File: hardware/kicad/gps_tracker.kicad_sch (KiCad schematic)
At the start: 16 parts, among them J1 GNSS: Foxeer M10Q-250 / Beiti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, J2 BIGGA GSM (SIM800C) board, J3 SSD1306 0.96" OLED I2C 0x3C, J4 MicroSD SPI module, J5 Battery Shield V8, 2x18650, J6 BMA400 CJMCU-400, J7 Button module, U1 ESP32-S3 SuperMini (ESP32-S3F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

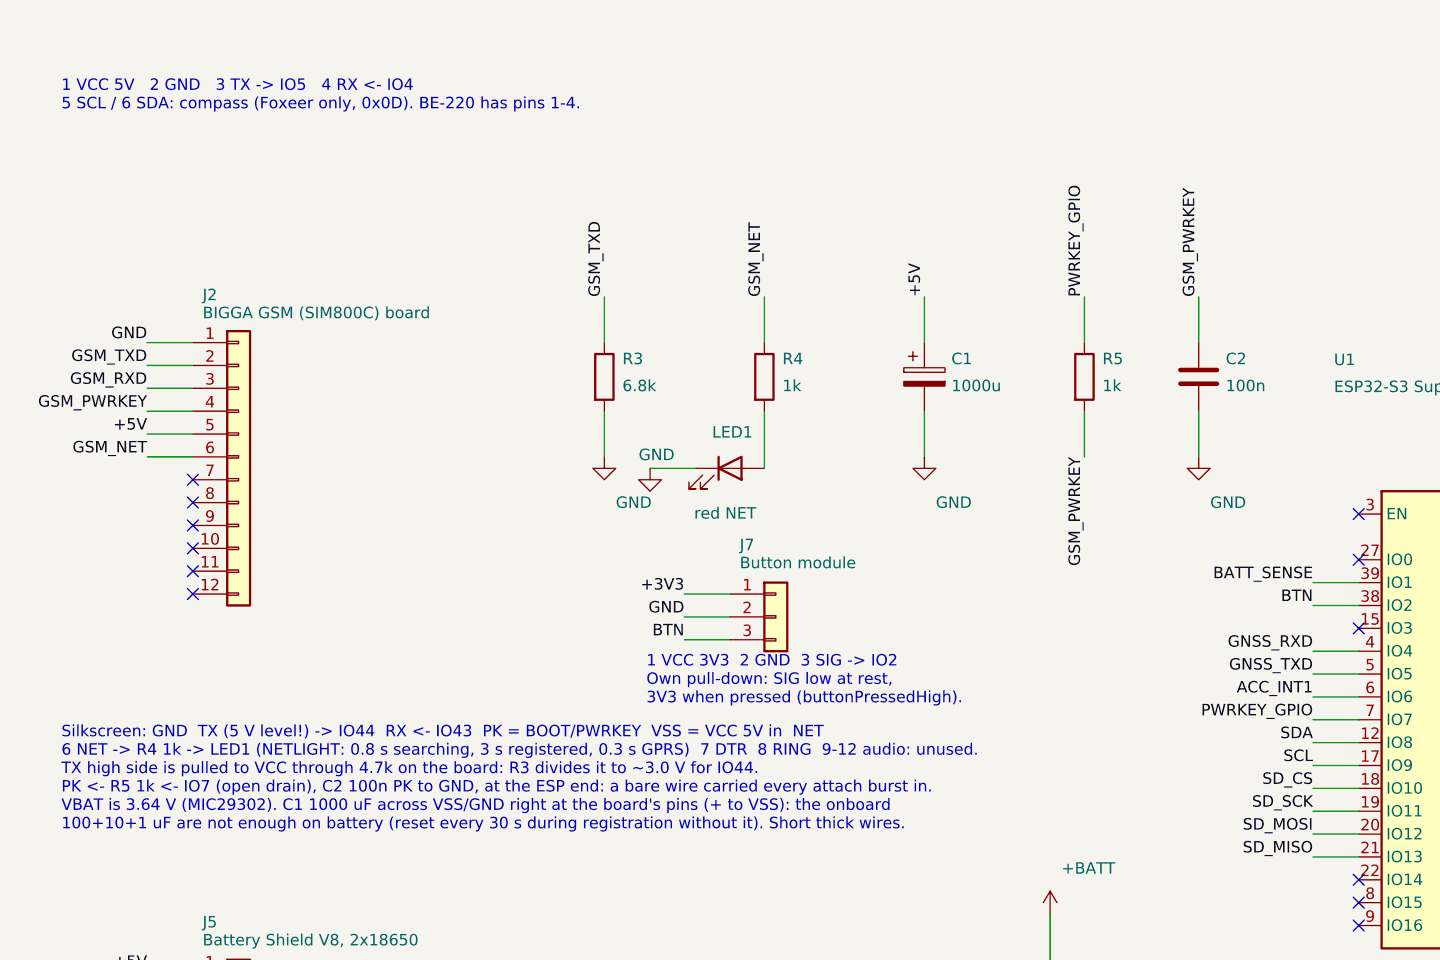
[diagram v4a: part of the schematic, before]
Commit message: Modem PWRKEY driven through an NPN transistor; drawings and documents follow
GPIO7 now drives the base of a 2N2222A through 10 kΩ, with 100 kΩ from
base to GND to keep it off while the ESP boots or sleeps; the emitter is
on GND and the collector pulls the modem's PWRKEY down. SIMCom's hardware
guide recommends this drive: nothing from the modem's line, neither the
attach bursts nor its ~4 V pull-up, reaches the ESP32 pin. Verified on
the bench with the modem powered off first: key pulse, 'Modem answered',
a fresh GPRS attach, no resets.

Config::gsmPowerKeyViaTransistor (true) inverts the drive: push-pull,
idle low, high for the 1.2 s pulse. false keeps the open-drain drive for
the RC-filter wiring (1 kΩ in series, 100 nF to GND), which also stopped
the resets. The boot log names the mode in use.

Schematic: Q1, R5 10k, R6 100k in place of R5 1k / C2 100n (ERC clean,
PDF and SVG re-exported). Wiring diagram, assembly sheet, both READMEs
and the changelog describe the transistor and keep the RC filter and
PWRKEY-to-GND as alternatives.
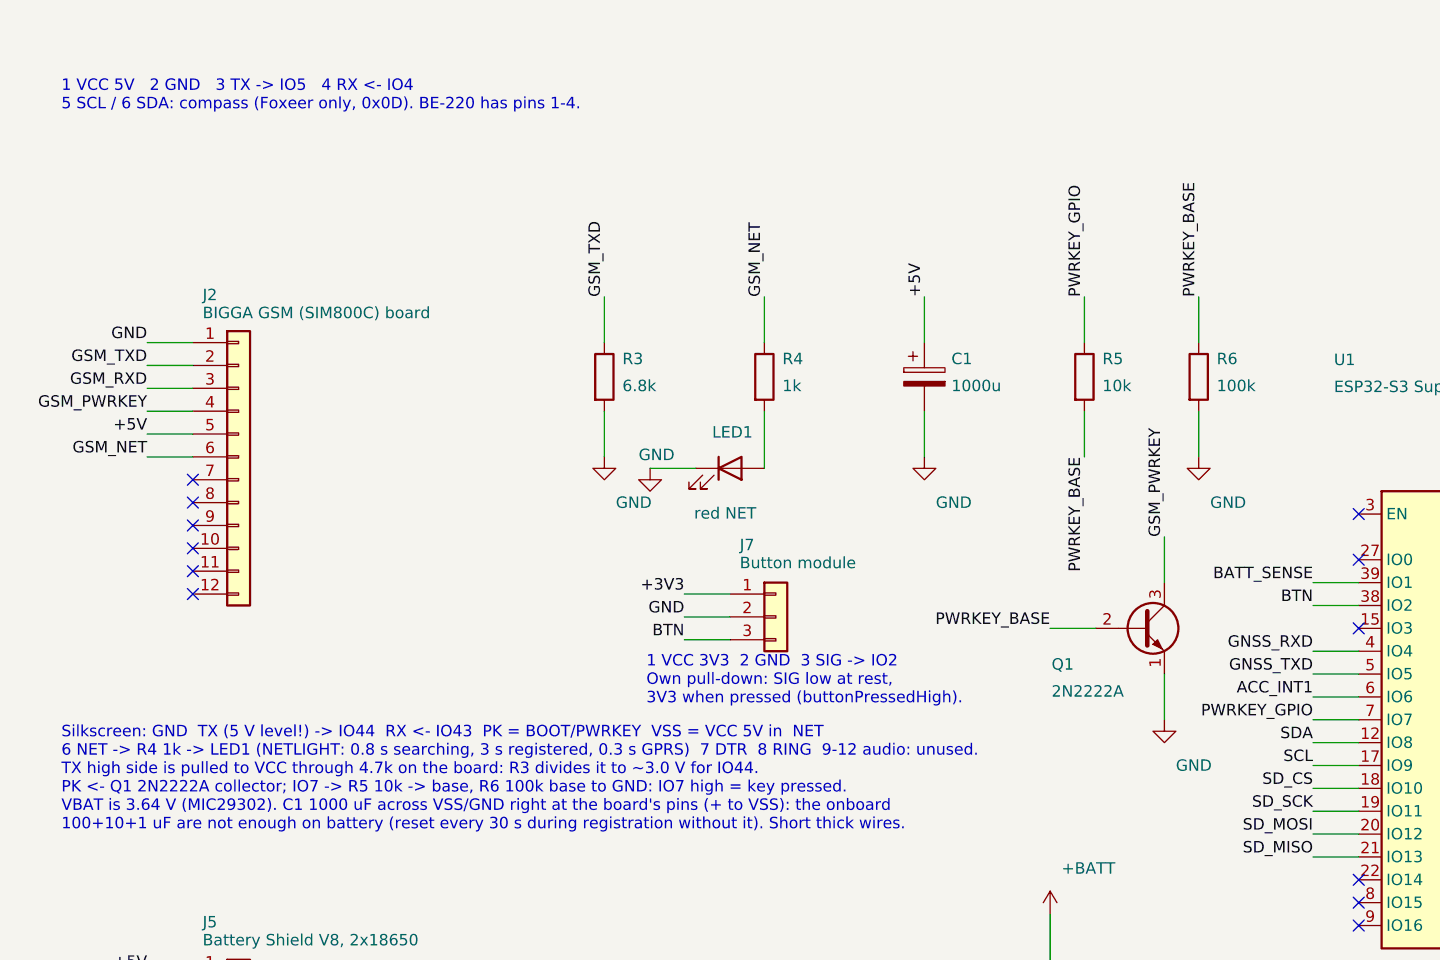
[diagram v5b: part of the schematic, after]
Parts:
- removed C2: 100n, symbol Device:C
- added Q1: 2N2222A, symbol Transistor_BJT:Q_NPN_EBC
- added R6: 100k, symbol Device:R
- R5: value 1k -> 10k
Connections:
- net GND: now also Q1.1 (E), R6.2
- net GSM_PWRKEY: now also Q1.3 (C); no longer R5.2
- new net PWRKEY_BASE: Q1.2 (B), R5.2, R6.1
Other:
- note added: "Silkscreen: GND TX (5 V level!) -> IO44 RX <- IO43 PK = BOOT/PWRKEY VSS = VCC 5V in NET 6 NET -> R4 1k -> LED1 (NETLIGHT: 0.8 s searching, 3 s registered, 0.3 s GPRS) 7 DTR 8 RING 9-12 audio: unused. TX high side is pulled to VCC through 4.7k on the board: R3 divides it to ~3.0 V for IO44. PK <- Q1 2N2222A collector; IO7 -> R5 10k -> base, R6 100k base to GND: IO7 high = key pressed. VBAT is 3.64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"
- note removed: "Silkscreen: GND TX (5 V level!) -> IO44 RX <- IO43 PK = BOOT/PWRKEY VSS = VCC 5V in NET 6 NET -> R4 1k -> LED1 (NETLIGHT: 0.8 s searching, 3 s registered, 0.3 s GPRS) 7 DTR 8 RING 9-12 audio: unused. TX high side is pulled to VCC through 4.7k on the board: R3 divides it to ~3.0 V for IO44. PK <- R5 1k <- IO7 (open drain), C2 100n PK to GND, at the ESP end: a bare wire carried every attach burst i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"
